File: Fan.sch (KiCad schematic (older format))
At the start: 0 parts

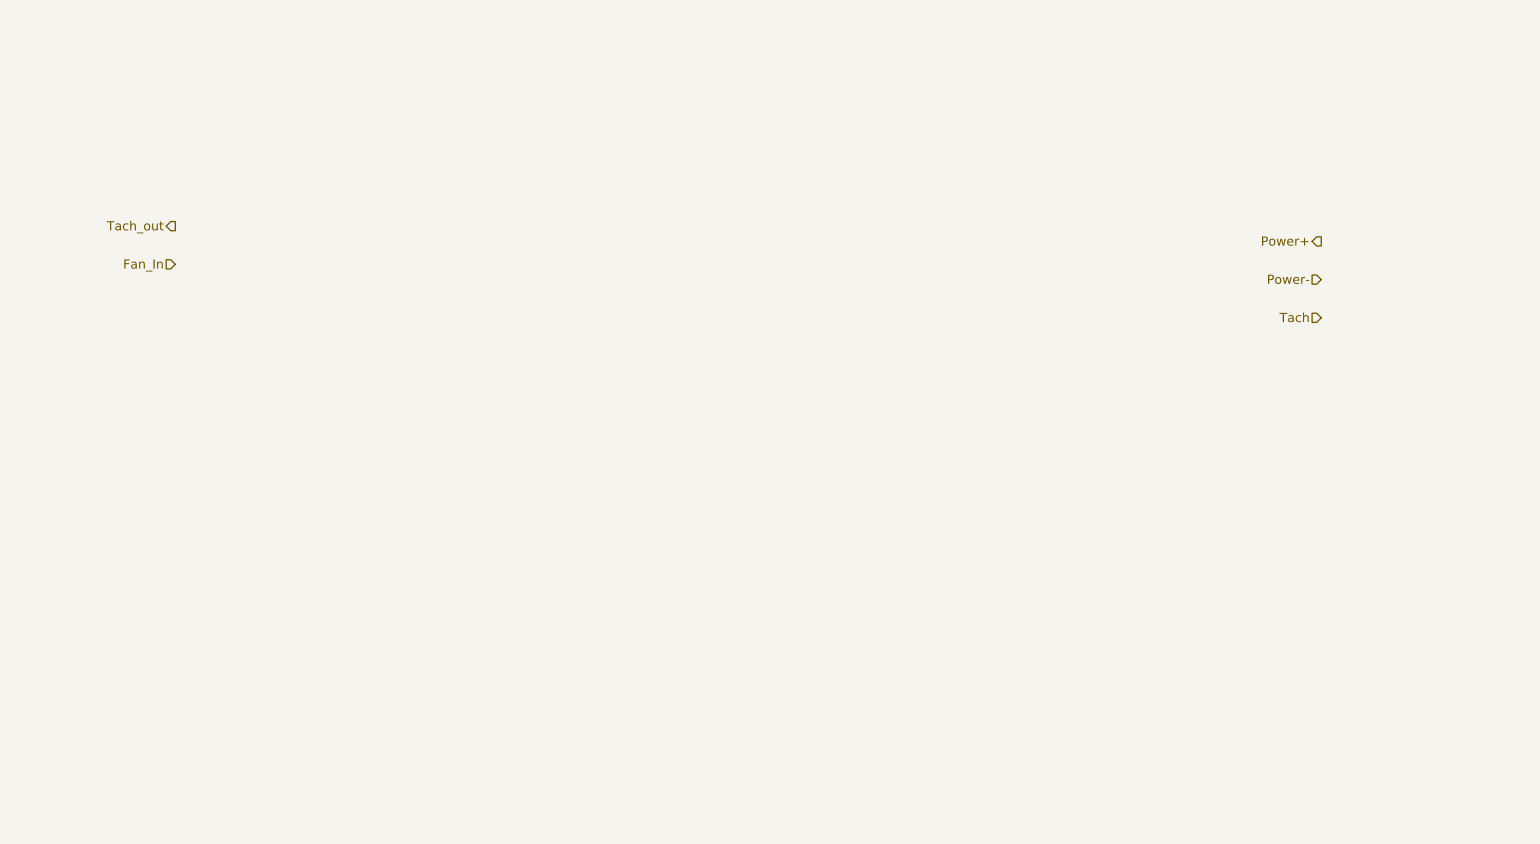
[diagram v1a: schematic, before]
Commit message: Module 3, Unit 4: Understanding The Current/Fan Driver Module
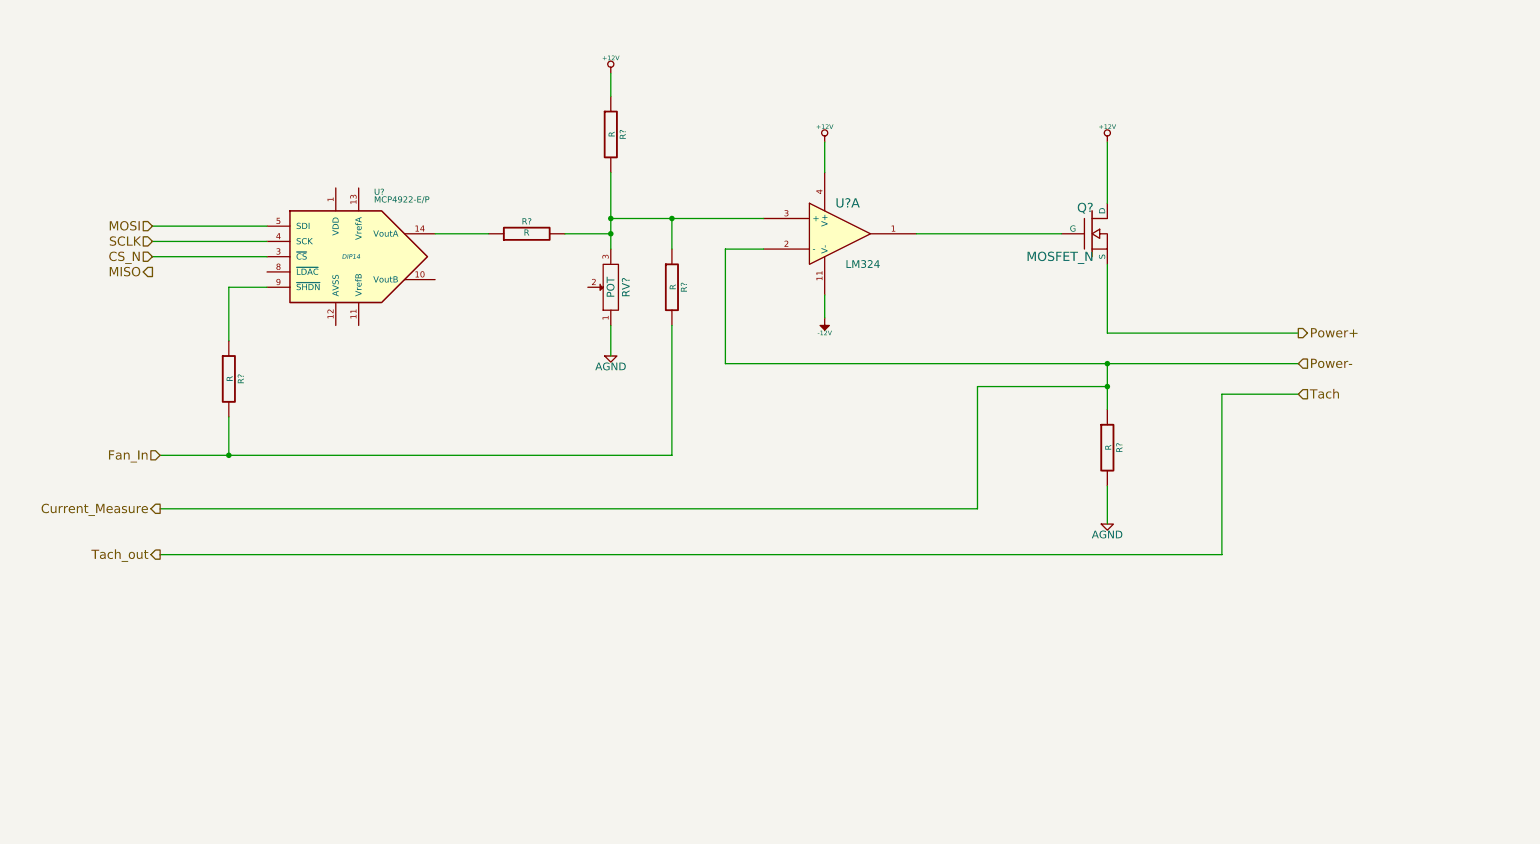
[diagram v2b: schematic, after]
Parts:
- added Q?: MOSFET_N, symbol MOSFET_N
- added R? (x5): R, symbol R
- added RV?: POT, symbol POT
- added U?: LM324, symbol LM324
- added U?: MCP4922-E/P, DIP14, symbol MCP4922-E/P
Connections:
- net Fan_In: now also R?.2, R?.2
- net Power+: now also Q?.S
- new net: Q?.G, U?.1
- new net: R?.1, R?.2, R?.2, RV?.3, U?.3 (+)
- new net: R?.1, U?.14 (VoutA)
- new net: R?.1, U?.9 (~SHDN~)
- new net +12V: Q?.D, R?.1, U?.4 (V+)
- new net -12V: U?.11 (V-)
- new net AGND: R?.2, RV?.1
- new net CS_N: U?.3 (~CS~)
- new net Current_Measure: R?.1, U?.2 (-)
- new net MOSI: U?.5 (SDI)
- new net SCLK: U?.4 (SCK)

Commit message: Module 3, Unit 9: Understanding The Arduino Module
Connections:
- net Current_Measure renamed CURR_MEAS
- net Fan_In renamed FAN_EN_N
- net Power+ renamed FAN_OUT+
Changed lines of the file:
@@
 $Descr A4 11693 8268
 encoding utf-8
-Sheet 7 9
+Sheet 8 9
 Title ""
 Date ""
@@
 $EndDescr
 Text HLabel 9100 3050 2    60   Output ~ 0
-Power+
-Text HLabel 9100 3250 2    60   Input ~ 0
-Power-
+FAN_OUT+
+Text HLabel 9100 3250 2    60   Output ~ 0
+FAN_OUT-
 Text HLabel 9100 3450 2    60   Input ~ 0
-Tach
+TACH_IN
 Text HLabel 1650 4500 0    60   Output ~ 0
-Tach_out
+TACH_MEAS
 Text HLabel 1650 3850 0    60   Input ~ 0
-Fan_In
+FAN_EN_N
 $Comp
 L LM324 U?
@@
 	8600 4500 1650 4500
 Text HLabel 1650 4200 0    60   Output ~ 0
-Current_Measure
+CURR_MEAS
 Wire Wire Line
 	1650 4200 7000 4200

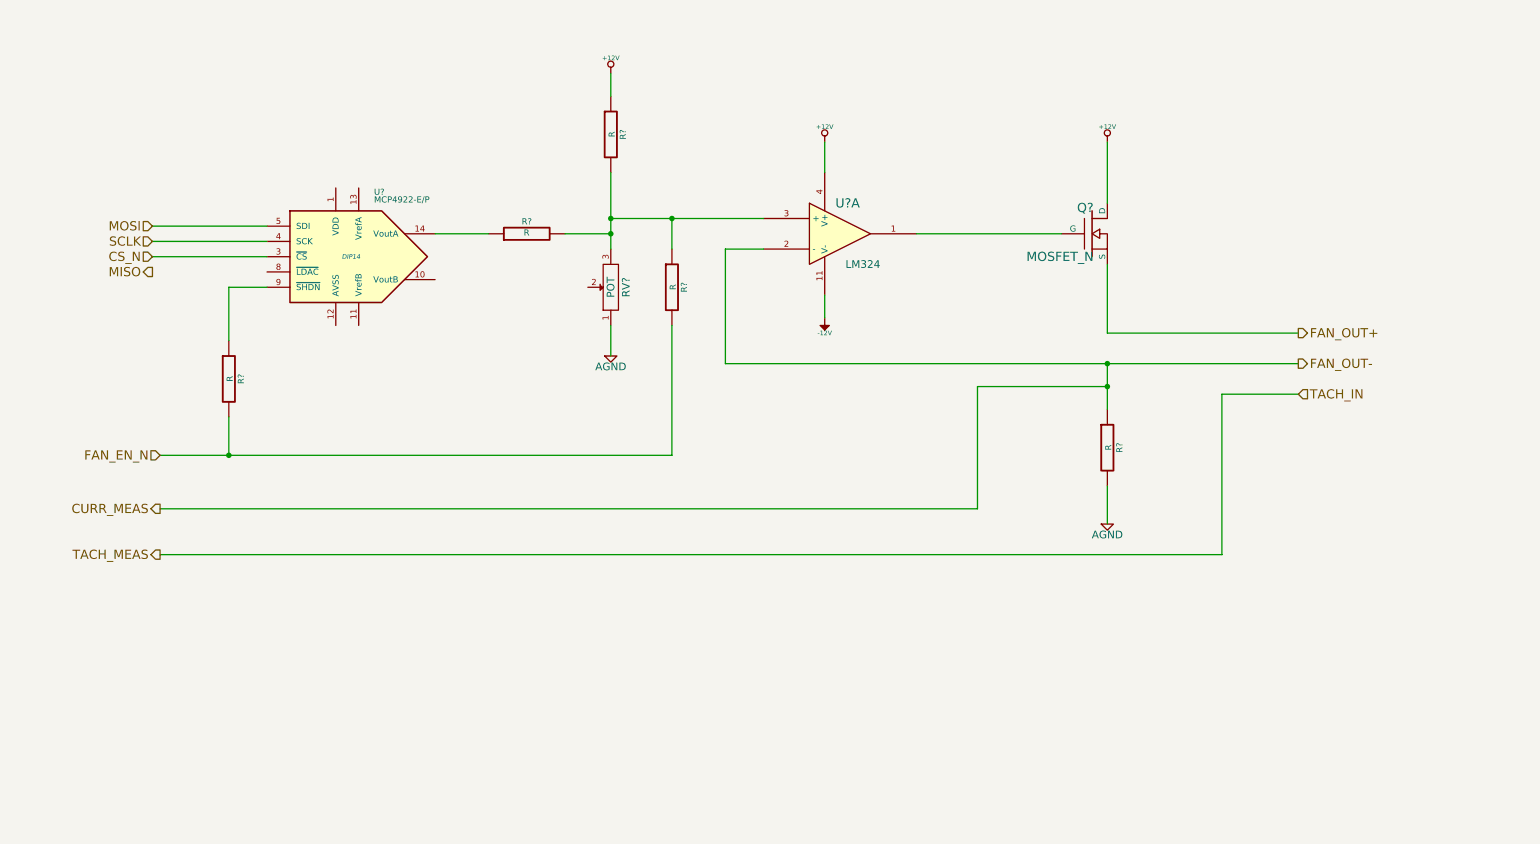
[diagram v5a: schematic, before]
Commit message: Module 3, Unit 10: Revisiting The Current/Fan Module
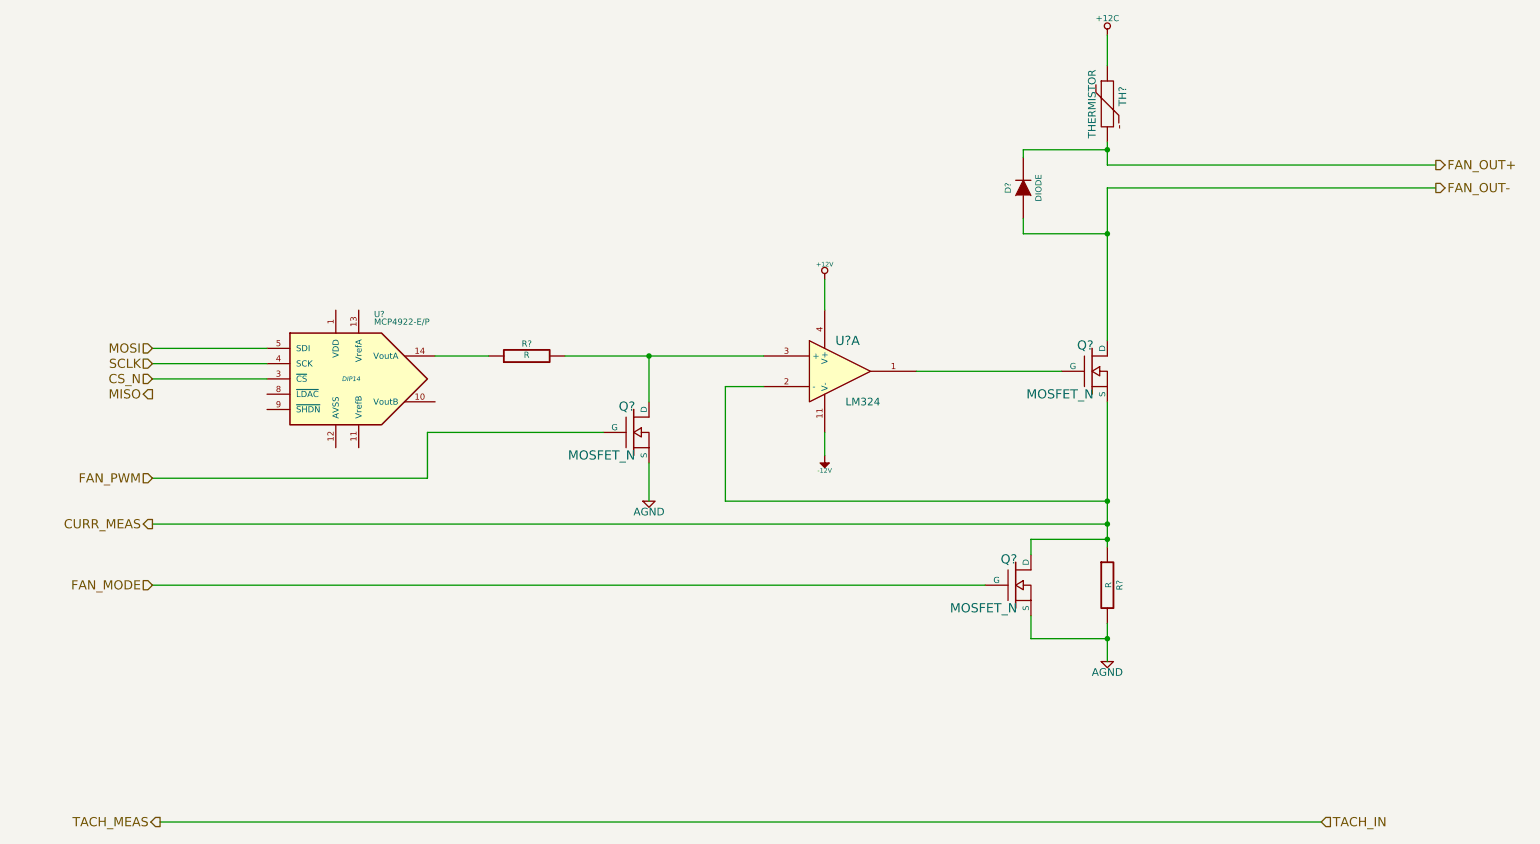
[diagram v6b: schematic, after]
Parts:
- removed R? (x3): R, symbol R
- removed RV?: POT, symbol POT
- added D?: DIODE, symbol DIODE
- added Q? (x2): MOSFET_N, symbol MOSFET_N
- added TH?: THERMISTOR, symbol THERMISTOR
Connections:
- net +12V: no longer Q?.D
- net AGND: now also Q?.S, Q?.S
- net CURR_MEAS: now also Q?.S, Q?.D
- net FAN_OUT+: now also D?.2 (K), TH?.2; no longer Q?.S
- net at R?.2, U?.3 (+): now also Q?.D
- new net +12C: TH?.1
- new net FAN_MODE: Q?.G
- new net FAN_OUT-: D?.1 (A), Q?.D
- new net FAN_PWM: Q?.G
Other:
- moved on the sheet: Q?, R?, U?, U?A
